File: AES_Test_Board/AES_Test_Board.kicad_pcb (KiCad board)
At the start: 2 copper layers, 14 parts, among them J1 Conn_02x06_Top_Bottom, J2 Conn_02x06_Top_Bottom, J4 Conn_01x01, J5 Conn_01x01

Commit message: Finished board
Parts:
- removed J4, J5: Conn_01x01, Connector:Banana_Jack_1Pin
- removed R10, R11, R12, R4, R5, R6, R7, R8, R9: 0, Resistor_SMD:R_0805_2012Metric
- added BSY1: BSY, TestPoint:TestPoint_Keystone_5000-5004_Miniature, F.Cu at (119.2, 63.3)
- added C1: .1u, Capacitor_SMD:C_0805_2012Metric_Pad1.18x1.45mm_HandSolder, F.Cu at (128.5, 97.8)
- added C10: 1u, Capacitor_SMD:C_0805_2012Metric_Pad1.18x1.45mm_HandSolder, F.Cu at (107.0, 86.0)
- added C2: 1u, Capacitor_SMD:C_0805_2012Metric_Pad1.18x1.45mm_HandSolder, F.Cu at (128.5, 95.3)
- added C3: 10u, Capacitor_SMD:C_0805_2012Metric_Pad1.18x1.45mm_HandSolder, F.Cu at (128.5, 92.8)
- added C4: .1u, Capacitor_SMD:C_0805_2012Metric_Pad1.18x1.45mm_HandSolder, F.Cu at (133.0, 97.8)
- added C5: 1u, Capacitor_SMD:C_0805_2012Metric_Pad1.18x1.45mm_HandSolder, F.Cu at (133.0, 95.3)
- added C6: 10u, Capacitor_SMD:C_0805_2012Metric_Pad1.18x1.45mm_HandSolder, F.Cu at (133.0, 92.8)
- added C7: 1u, Capacitor_SMD:C_0805_2012Metric_Pad1.18x1.45mm_HandSolder, F.Cu at (107.0, 97.0)
- added C8: 1u, Capacitor_SMD:C_0805_2012Metric_Pad1.18x1.45mm_HandSolder, F.Cu at (107.0, 89.0)
- added C9: 1u, Capacitor_SMD:C_0805_2012Metric_Pad1.18x1.45mm_HandSolder, F.Cu at (107.0, 100.0)
- added CLK1: CLK, TestPoint:TestPoint_Keystone_5000-5004_Miniature, F.Cu at (119.2, 73.8)
- added CLKOUT1: CLKOUT, TestPoint:TestPoint_Keystone_5000-5004_Miniature, F.Cu at (119.2, 112.3)
- added DRDY1: DRDY, TestPoint:TestPoint_Keystone_5000-5004_Miniature, F.Cu at (119.2, 66.8)
- added EN1: EN, TestPoint:TestPoint_Keystone_5000-5004_Miniature, F.Cu at (119.2, 77.3)
- added KRDY1: KRDY, TestPoint:TestPoint_Keystone_5000-5004_Miniature, F.Cu at (119.2, 70.3)
- added RSTN1: RSTN, TestPoint:TestPoint_Keystone_5000-5004_Miniature, F.Cu at (119.2, 80.8)
- added SCLK1: SCLK, TestPoint:TestPoint_Keystone_5000-5004_Miniature, F.Cu at (119.2, 94.8)
- added SE1: SE, TestPoint:TestPoint_Keystone_5000-5004_Miniature, F.Cu at (119.2, 87.8)
- added SI1: SI, TestPoint:TestPoint_Keystone_5000-5004_Miniature, F.Cu at (119.2, 84.3)
- added SO1: SO, TestPoint:TestPoint_Keystone_5000-5004_Miniature, F.Cu at (119.2, 91.3)
- added SU1: SU, TestPoint:TestPoint_Keystone_5000-5004_Miniature, F.Cu at (119.2, 98.3)
- added U2: TLV74010PDBVR, Package_TO_SOT_SMD:SOT-23-5, F.Cu at (107.0, 93.0)
- added VDDD1: VDDD, TestPoint:TestPoint_Keystone_5000-5004_Miniature, F.Cu at (119.2, 101.8)
- added VDDPST1: VDDPST, TestPoint:TestPoint_Keystone_5000-5004_Miniature, F.Cu at (119.2, 108.8)
- added VSS1: VSS, TestPoint:TestPoint_Keystone_5000-5004_Miniature, F.Cu at (119.2, 105.3)
- moved U1 16.3 mm to (135.0, 86.5)
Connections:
- J1 pad 1: /SCAN_IN -> /BSY
- J1 pad 10: /BSY -> /SCAN_ENABLE
- J1 pad 12: /VDD -> /VDDPST
- J1 pad 2: /SCAN_ENABLE -> /KRDY
- J1 pad 3: /SCAN_UPDATE -> /ENABLE
- J1 pad 4: /SCAN_CLK -> /SCAN_IN
- J1 pad 6: /VDD -> /VDDPST
- J1 pad 7: /SCAN_OUT -> /DRDY
- J1 pad 8: /RSTN -> /CLK
- J1 pad 9: /ENABLE -> /RSTN
- J2 pad 1: /KRDY -> /SCAN_OUT
- J2 pad 2: /DRDY -> /SCAN_CLK
- J2 pad 3: /CLK -> /SCAN_UPDATE
- J2 pad 4: /CLKOUT -> unconnected-(J2-Pin_4-Pad4)
- U1 pad 1: /VSSPST -> /VSS
- U1 pad 44: Net-(U1-AES_Drdy) -> /DRDY
- U1 pad 45: Net-(U1-AES_Krdy) -> /KRDY
- U1 pad 46: Net-(U1-AES_CLK) -> /CLK
- U1 pad 47: Net-(U1-AES_ENABLE) -> /ENABLE
- U1 pad 48: Net-(U1-AES_RSTN) -> /RSTN
- U1 pad 49: Net-(U1-AES_SCAN_IN) -> /SCAN_IN
- U1 pad 50: Net-(U1-AES_SCAN_ENABLE) -> /SCAN_ENABLE
- U1 pad 52: Net-(U1-AES_SCAN_CLK) -> /SCAN_CLK
- U1 pad 53: Net-(U1-AES_SCAN_UPDATE) -> /SCAN_UPDATE
- U1 pad 55: /VDD -> /VDDD
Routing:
- net /VDDPST: track 0.00 -> 78.1 mm
- net /BSY: track 0.00 -> 55.2 mm
- net /DRDY: track 0.00 -> 48.5 mm
- net /KRDY: track 0.00 -> 47.7 mm
- net /SCAN_UPDATE: track 0.00 -> 43.4 mm
- net /ENABLE: track 0.00 -> 43.0 mm
- net /SCAN_CLK: track 0.00 -> 42.5 mm
- net /SCAN_IN: track 0.00 -> 41.8 mm
- net /SCAN_OUT: track 0.00 -> 41.7 mm
- net /CLK: track 0.00 -> 40.8 mm
- net /SCAN_ENABLE: track 0.00 -> 39.5 mm
- net /RSTN: track 0.00 -> 39.4 mm
- net /VDDD: track 0.00 -> 39.2 mm
- net /CLKOUT: track 0.00 -> 27.6 mm
- net Net-(U1-AES_SCAN_UPDATE): track 14.8 -> 0.00 mm
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- added copper zone on B.Cu, net /VSS
- added copper zone on F.Cu, net /VSS
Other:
- board outline added: 55 x 55 mm

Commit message: Emulation Board bitstream works
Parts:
- added G***: LOGO, Connector:mohit, F.Cu at (131.0, 67.0)
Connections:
- U1 pad 54: unconnected-(U1-VDDPOC-Pad54) -> /VDDPST
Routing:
- net /VDDPST: track 78.1 -> 103.6 mm, vias 0 -> 1

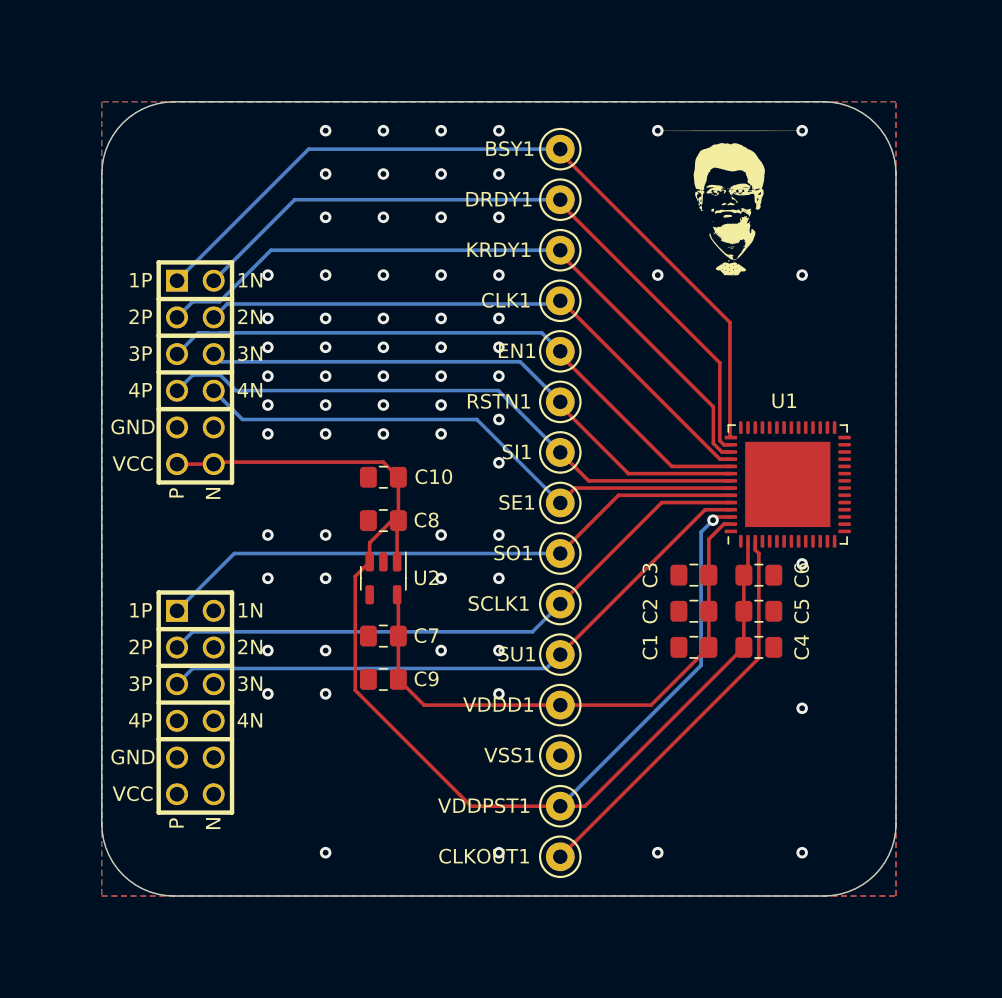
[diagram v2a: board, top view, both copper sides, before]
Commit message: Created new vivado project that has both test and emulation synthesizable code within it. Also changed PCB to match professors input
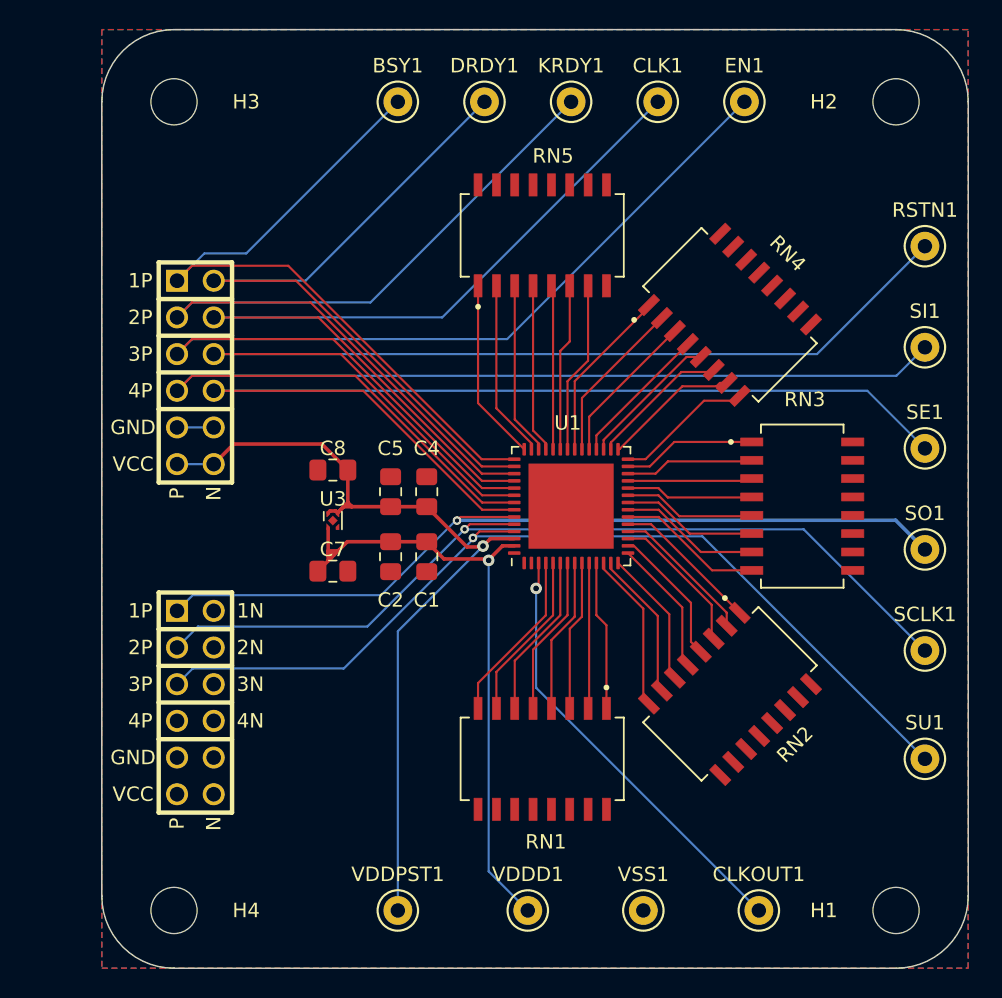
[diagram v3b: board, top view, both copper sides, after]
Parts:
- removed C10, C9: 1u, Capacitor_SMD:C_0805_2012Metric_Pad1.18x1.45mm_HandSolder
- removed C3, C6: 10u, Capacitor_SMD:C_0805_2012Metric_Pad1.18x1.45mm_HandSolder
- removed G***: LOGO, Connector:mohit
- removed U2: TLV74010PDBVR, Package_TO_SOT_SMD:SOT-23-5
- added H1: MountingHole, MountingHole:MountingHole_3.2mm_M3, F.Cu at (142.5, 116.0)
- added H2: MountingHole, MountingHole:MountingHole_3.2mm_M3, F.Cu at (142.5, 60.0)
- added H3: MountingHole, MountingHole:MountingHole_3.2mm_M3, F.Cu at (92.5, 60.0)
- added H4: MountingHole, MountingHole:MountingHole_3.2mm_M3, F.Cu at (92.5, 116.0)
- added RN1: 4816P-1-104LF, Connector:SOIC127P762X240-16N, F.Cu at (118.0, 105.5)
- added RN2: 4816P-1-104LF, Connector:SOIC127P762X240-16N, F.Cu at (131.0, 101.0)
- added RN3: 4816P-1-104LF, Connector:SOIC127P762X240-16N, F.Cu at (136.0, 88.0)
- added RN4: 4816P-1-104LF, Connector:SOIC127P762X240-16N, F.Cu at (131.0, 74.8)
- added RN5: 4816P-1-104LF, Connector:SOIC127P762X240-16N, F.Cu at (118.0, 69.2)
- added U3: TCR3RM10A, Package_DFN_QFN:UDFN-4-1EP_1x1mm_P0.65mm_EP0.48x0.48mm, F.Cu at (103.5, 89.0)
- moved RSTN1 27.5 mm to (144.5, 70.0)
- moved C5 26.8 mm to (107.5, 87.0), turned to 90 degrees
- moved SI1 26.3 mm to (144.5, 77.0)
- moved SU1 26.3 mm to (144.5, 105.5)
- moved SE1 25.5 mm to (144.5, 84.0)
- moved SCLK1 25.5 mm to (144.5, 98.0)
- moved C4 25.4 mm to (110.0, 87.0), turned to 90 degrees
- moved SO1 25.3 mm to (144.5, 91.0)
- moved EN1 21.5 mm to (132.0, 60.0)
- moved C2 21.3 mm to (107.5, 91.5), turned to -90 degrees
- moved C1 19.5 mm to (110.0, 91.5), turned to -90 degrees
- moved CLK1 15.3 mm to (126.0, 60.0)
- moved U1 15.1 mm to (120.0, 88.0)
- moved VDDD1 14.4 mm to (117.0, 116.0)
- moved CLKOUT1 14.2 mm to (133.0, 116.0)
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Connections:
- U1 pad 10: (no net) -> /MLPIN10
- U1 pad 11: (no net) -> /MLPIN11
- U1 pad 12: (no net) -> /MLPIN12
- U1 pad 13: (no net) -> /MLPIN13
- U1 pad 14: (no net) -> /MLPIN14
- U1 pad 15: (no net) -> /MLPIN15
- U1 pad 16: (no net) -> /MLPIN16
- U1 pad 17: (no net) -> /MLPIN17
- U1 pad 18: (no net) -> /MLPIN18
- U1 pad 19: (no net) -> /MLPIN19
- U1 pad 20: (no net) -> /MLPIN20
- U1 pad 21: (no net) -> /MLPIN21
- U1 pad 22: (no net) -> /MLPIN22
- U1 pad 23: (no net) -> /MLPIN23
- U1 pad 24: (no net) -> /MLPIN24
- U1 pad 25: (no net) -> /MLPIN25
- U1 pad 26: (no net) -> /MLPIN26
- U1 pad 27: (no net) -> /MLPIN27
- U1 pad 28: (no net) -> /MLPIN28
- U1 pad 29: (no net) -> /MLPIN29
- U1 pad 30: (no net) -> /MLPIN30
- U1 pad 31: (no net) -> /MLPIN31
- U1 pad 32: (no net) -> /MLPIN32
- U1 pad 33: (no net) -> /MLPIN33
- U1 pad 34: (no net) -> /MLPIN34
- U1 pad 35: (no net) -> /MLPIN35
- U1 pad 36: (no net) -> /MLPIN36
- U1 pad 37: (no net) -> /MLPIN37
- U1 pad 38: (no net) -> /MLPIN38
- U1 pad 39: (no net) -> /MLPIN39
- U1 pad 4: (no net) -> /MLPIN4
- U1 pad 40: (no net) -> /MLPIN40
- U1 pad 41: (no net) -> /MLPIN41
- U1 pad 42: (no net) -> /MLPIN42
- U1 pad 5: (no net) -> /MLPIN5
- U1 pad 6: (no net) -> /MLPIN6
- U1 pad 7: (no net) -> /MLPIN7
- U1 pad 8: (no net) -> /MLPIN8
- U1 pad 9: (no net) -> /MLPIN9
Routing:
- net /VDDPST: track 103.6 -> 59.0 mm
- net /SCAN_IN: track 41.8 -> 80.5 mm
- net /RSTN: track 39.4 -> 77.2 mm
- net /SCAN_ENABLE: track 39.5 -> 75.1 mm
- net /ENABLE: track 43.0 -> 74.6 mm
- net /SCAN_UPDATE: track 43.4 -> 65.8 mm, vias 0 -> 1
- net /CLK: track 40.8 -> 62.4 mm
- net /SCAN_CLK: track 42.5 -> 62.2 mm, vias 0 -> 1
- net /SCAN_OUT: track 41.7 -> 59.3 mm, vias 0 -> 1
- net /KRDY: track 47.7 -> 62.2 mm
- net /MLPIN42: track 0.00 -> 12.6 mm
- net /MLPIN41: track 0.00 -> 12.3 mm
- net /MLPIN35: track 0.00 -> 12.1 mm
- net /MLPIN4: track 0.00 -> 12.0 mm
- net /MLPIN40: track 0.00 -> 12.0 mm
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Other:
- board size 55 x 55 mm -> 60 x 65 mm

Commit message: Combined fpga works
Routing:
- net /RSTN: track 77.2 -> 77.5 mm, vias 0 -> 1
- net /VSS: vias 0 -> 23
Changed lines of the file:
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@@
   (gr_arc (start 142.5 55) (mid 146.035534 56.464466) (end 147.5 60)
     (stroke (width 0.1) (type default)) (layer "Edge.Cuts"))
+  (dimension (type aligned) (layer "B.Cu")
+    (pts (xy 92.5 55) (xy 92.5 120))
+    (height 21.2)
+    (gr_text "65.0000 mm" (at 69.5 87.5 90) (layer "B.Cu")
+      (effects (font (size 1.5 1.5) (thickness 0.3)))
+    )
+    (format (prefix "") (suffix "") (units 3) (units_format 1) (precision 4))
+    (style (thickness 0.2) (arrow_length 1.27) (text_position_mode 0) (extension_height 0.58642) (extension_offset 0.5) keep_text_aligned)
+  )
+  (dimension (type aligned) (layer "B.Cu")
+    (pts (xy 92.5 60) (xy 142.5 60))
+    (height -7)
+    (gr_text "50.0000 mm" (at 117.5 51.2) (layer "B.Cu")
+      (effects (font (size 1.5 1.5) (thickness 0.3)))
+    )
+    (format (prefix "") (suffix "") (units 3) (units_format 1) (precision 4))
+    (style (thickness 0.2) (arrow_length 1.27) (text_position_mode 0) (extension_height 0.58642) (extension_offset 0.5) keep_text_aligned)
+  )
+  (dimension (type aligned) (layer "B.Cu")
+    (pts (xy 87.5 60) (xy 147.5 60))
+    (height -11.3)
+    (gr_text "60.0000 mm" (at 117.5 46.9) (layer "B.Cu")
+      (effects (font (size 1.5 1.5) (thickness 0.3)))
+    )
+    (format (prefix "") (suffix "") (units 3) (units_format 1) (precision 4))
+    (style (thickness 0.2) (arrow_length 1.27) (text_position_mode 0) (extension_height 0.58642) (extension_offset 0.5) keep_text_aligned)
+  )
+  (dimension (type aligned) (layer "B.Cu")
+    (pts (xy 92.5 60) (xy 92.5 116))
+    (height 18.2)
+    (gr_text "56.0000 mm" (at 72.5 88 90) (layer "B.Cu")
+      (effects (font (size 1.5 1.5) (thickness 0.3)))
+    )
+    (format (prefix "") (suffix "") (units 3) (units_format 1) (precision 4))
+    (style (thickness 0.2) (arrow_length 1.27) (text_position_mode 0) (extension_height 0.58642) (extension_offset 0.5) keep_text_aligned)
+  )
   (dimension (type aligned) (layer "Cmts.User")
     (pts (xy 95.25 85.09) (xy 95.25 95.25))
@@
   (segment (start 136.102586 89.602586) (end 144.5 98) (width 0.15) (layer "B.Cu") (net 4))
   (segment (start 112.624876 89.602586) (end 136.102586 89.602586) (width 0.15) (layer "B.Cu") (net 4))
+  (via (at 100 95) (size 0.8) (drill 0.4) (layers "F.Cu" "B.Cu") (free) (net 5))
+  (via (at 140 95) (size 0.8) (drill 0.4) (layers "F.Cu" "B.Cu") (free) (net 5))
+  (via (at 110 65) (size 0.8) (drill 0.4) (layers "F.Cu" "B.Cu") (free) (net 5))
+  (via (at 120 105) (size 0.8) (drill 0.4) (layers "F.Cu" "B.Cu") (free) (net 5))
+  (via (at 110 115) (size 0.8) (drill 0.4) (layers "F.Cu" "B.Cu") (free) (net 5))
+  (via (at 90 65) (size 0.8) (drill 0.4) (layers "F.Cu" "B.Cu") (free) (net 5))
+  (via (at 110 105) (size 0.8) (drill 0.4) (layers "F.Cu" "B.Cu") (free) (net 5))
+  (via (at 140 105) (size 0.8) (drill 0.4) (layers "F.Cu" "B.Cu") (free) (net 5))
+  (via (at 90 95) (size 0.8) (drill 0.4) (layers "F.Cu" "B.Cu") (free) (net 5))
+  (via (at 140 115) (size 0.8) (drill 0.4) (layers "F.Cu" "B.Cu") (free) (net 5))
+  (via (at 100 85) (size 0.8) (drill 0.4) (layers "F.Cu" "B.Cu") (free) (net 5))
+  (via (at 120 115) (size 0.8) (drill 0.4) (layers "F.Cu" "B.Cu") (free) (net 5))
+  (via (at 90 115) (size 0.8) (drill 0.4) (layers "F.Cu" "B.Cu") (free) (net 5))
+  (via (at 130 65) (size 0.8) (drill 0.4) (layers "F.Cu" "B.Cu") (free) (net 5))
+  (via (at 100 105) (size 0.8) (drill 0.4) (layers "F.Cu" "B.Cu") (free) (net 5))
+  (via (at 100 115) (size 0.8) (drill 0.4) (layers "F.Cu" "B.Cu") (free) (net 5))
+  (via (at 90 105) (size 0.8) (drill 0.4) (layers "F.Cu" "B.Cu") (free) (net 5))
+  (via (at 130 115) (size 0.8) (drill 0.4) (layers "F.Cu" "B.Cu") (free) (net 5))
+  (via (at 90 75) (size 0.8) (drill 0.4) (layers "F.Cu" "B.Cu") (free) (net 5))
+  (via (at 100 65) (size 0.8) (drill 0.4) (layers "F.Cu" "B.Cu") (free) (net 5))
+  (via (at 90 85) (size 0.8) (drill 0.4) (layers "F.Cu" "B.Cu") (free) (net 5))
+  (via (at 140 65) (size 0.8) (drill 0.4) (layers "F.Cu" "B.Cu") (free) (net 5))
+  (via (at 130 75) (size 0.8) (drill 0.4) (layers "F.Cu" "B.Cu") (free) (net 5))
   (segment (start 92.71 82.55) (end 95.25 82.55) (width 0.15) (layer "B.Cu") (net 5))
   (segment (start 112.349503 88.75) (end 116.0625 88.75) (width 0.15) (layer "F.Cu") (net 6))
@@
   (segment (start 113.83241 87.25) (end 104.05241 77.47) (width 0.15) (layer "F.Cu") (net 7))
   (segment (start 104.05241 77.47) (end 95.25 77.47) (width 0.15) (layer "F.Cu") (net 7))
-  (segment (start 137.03 77.47) (end 144.5 70) (width 0.15) (layer "B.Cu") (net 7))
+  (via (at 140 75) (size 0.8) (drill 0.4) (layers "F.Cu" "B.Cu") (net 7))
+  (segment (start 139.5 75) (end 140 75) (width 0.15) (layer "B.Cu") (net 7))
+  (segment (start 140 75) (end 140 74.5) (width 0.15) (layer "B.Cu") (net 7))
+  (segment (start 140 74.5) (end 144.5 70) (width 0.15) (layer "B.Cu") (net 7))
+  (segment (start 137.03 77.47) (end 139.5 75) (width 0.15) (layer "B.Cu") (net 7))
   (segment (start 95.25 77.47) (end 137.03 77.47) (width 0.15) (layer "B.Cu") (net 7))
   (segment (start 103.510384 76.433) (end 93.747 76.433) (width 0.15) (layer "F.Cu") (net 8))

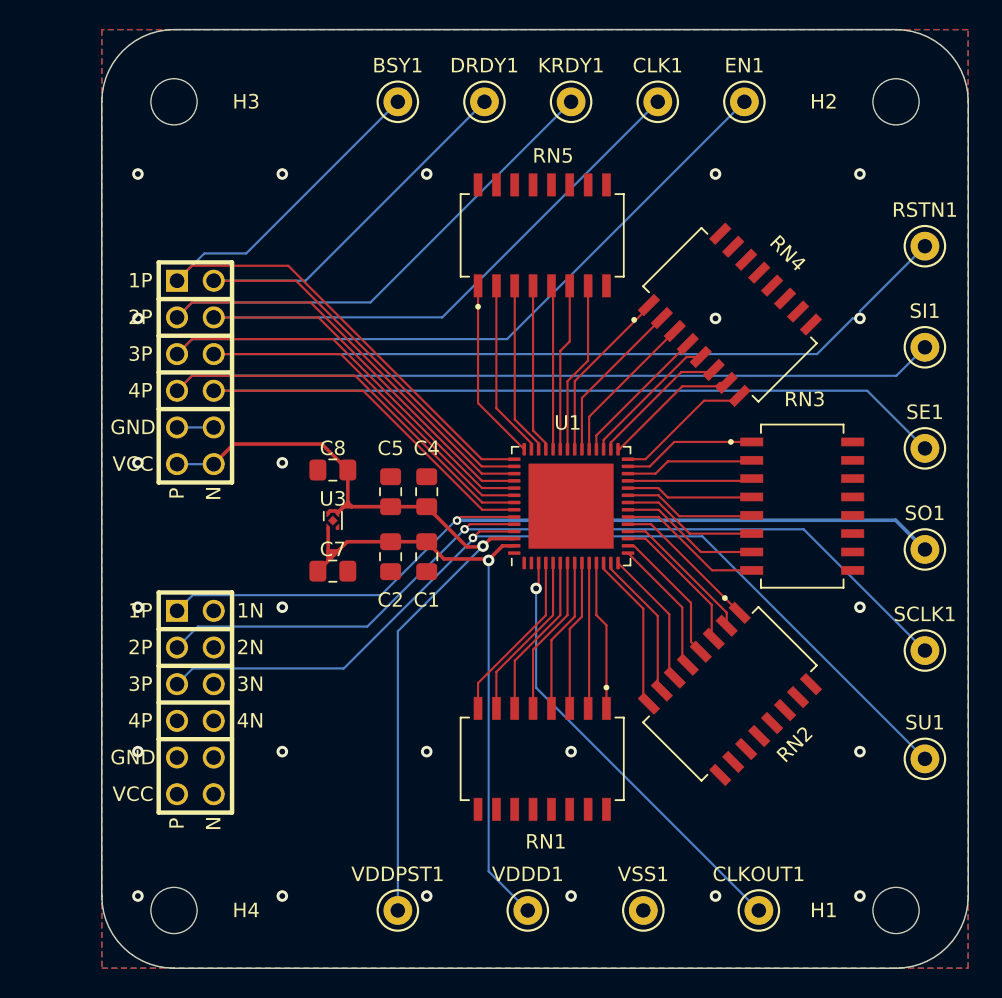
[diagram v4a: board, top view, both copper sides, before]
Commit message: Added 3 capacitors per power rail and changed pads to 0603
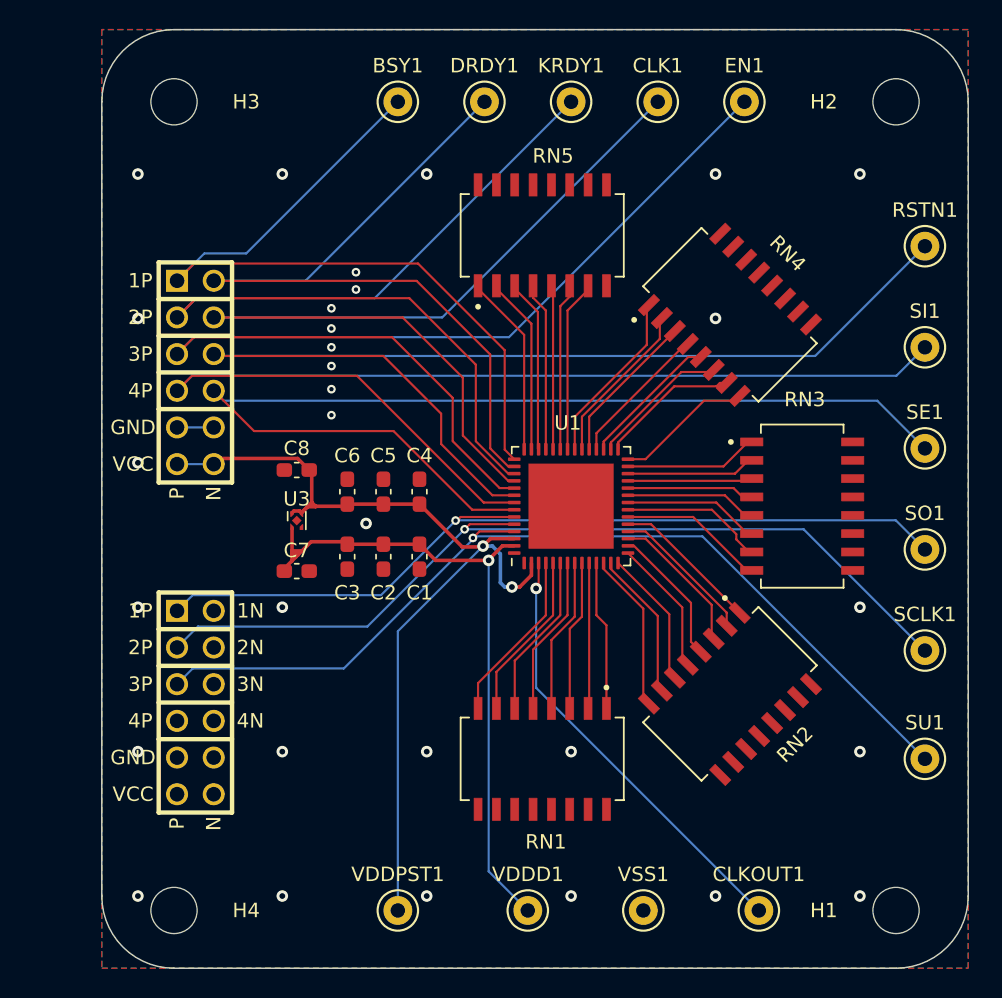
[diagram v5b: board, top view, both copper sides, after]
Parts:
- added C3: .01u, Capacitor_SMD:C_0603_1608Metric_Pad1.08x0.95mm_HandSolder, F.Cu at (104.5, 91.5)
- added C6: .01u, Capacitor_SMD:C_0603_1608Metric_Pad1.08x0.95mm_HandSolder, F.Cu at (104.5, 87.0)
- C1, C2, C4, C5, C7, C8: footprint Capacitor_SMD:C_0805_2012Metric_Pad1.18x1.45mm_HandSolder -> Capacitor_SMD:C_0603_1608Metric_Pad1.08x0.95mm_HandSolder
- moved C7 2.50 mm to (101.0, 92.5)
- moved C8 2.50 mm to (101.0, 85.5)
- moved U3 2.50 mm to (101.0, 89.0)
- moved C1 0.50 mm to (109.5, 91.5)
- moved C2 0.50 mm to (107.0, 91.5)
- moved C4 0.50 mm to (109.5, 87.0)
- moved C5 0.50 mm to (107.0, 87.0)
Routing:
- net /VDDPST: track 59.0 -> 65.3 mm, vias 1 -> 2
- net /BSY: track 49.8 -> 53.9 mm
- net /DRDY: track 50.0 -> 53.8 mm
- net /KRDY: track 62.2 -> 65.5 mm
- net /VDDD: track 44.5 -> 47.1 mm
- net /CLK: track 62.4 -> 64.8 mm
- net /ENABLE: track 74.6 -> 76.4 mm
- net /RSTN: track 77.5 -> 78.5 mm, vias 1 -> 0
- net /VSS: vias 23 -> 31
